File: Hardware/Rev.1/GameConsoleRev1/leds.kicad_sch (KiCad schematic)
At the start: 18 parts

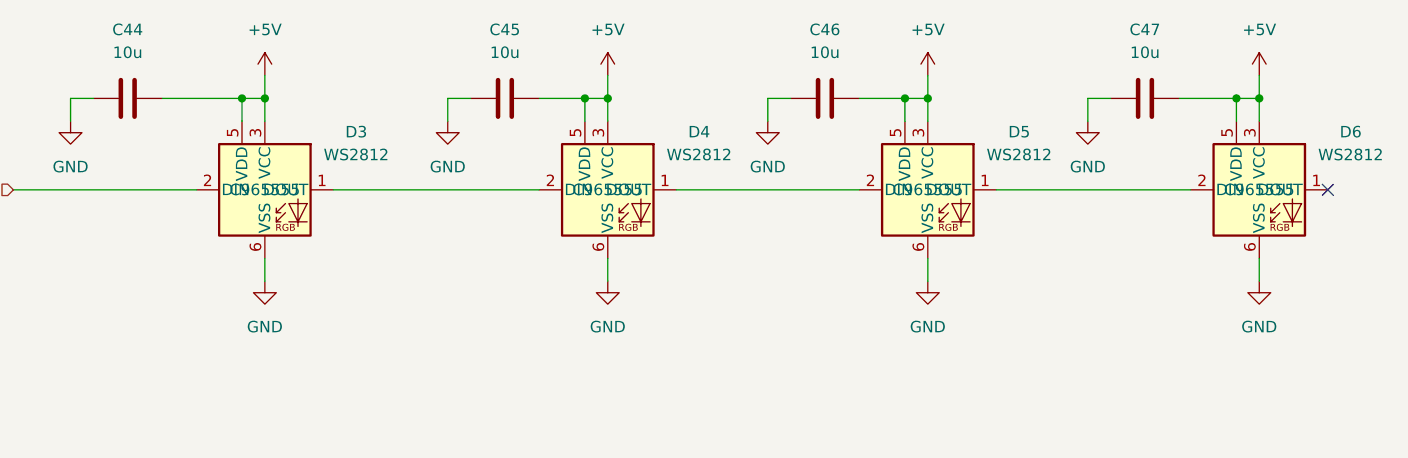
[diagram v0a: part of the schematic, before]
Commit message: Added CPP Build
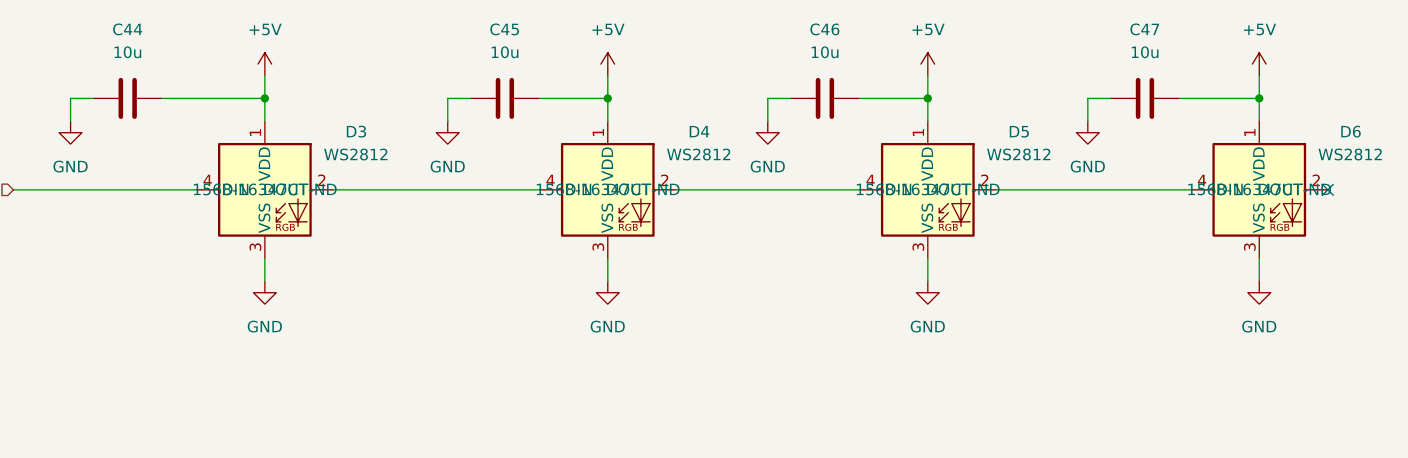
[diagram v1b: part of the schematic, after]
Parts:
- D12: footprint LED_SMD:LED_0603_1608Metric -> LED_SMD:LED_0805_2012Metric; DK# C566D-BFE-CU0W0351-ND -> 3147-B1701USD-20D000114U1930CT-ND
- D13, D14: footprint LED_SMD:LED_0603_1608Metric -> LED_SMD:LED_0805_2012Metric; DK# C566D-BFE-CU0W0351-ND -> 3147-B1701NG--20D000314U1930CT-ND
- D15, D16: footprint LED_SMD:LED_0603_1608Metric -> LED_SMD:LED_0805_2012Metric; DK# C566D-BFE-CU0W0351-ND -> 3147-B1701UD--20D000414U1930CT-ND
- D3, D4, D5, D6: footprint LED_SMD:LED_WS2812_PLCC6_5.0x5.0mm_P1.6mm -> LED_SMD:LED_WS2812B_PLCC4_5.0x5.0mm_P3.2mm; symbol LED:WS2812 -> LED:WS2812B; DK# (none) -> 1568-16347CT-ND; LCSC C965555 -> (none)
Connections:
- net +5V: now also D3.1 (VDD), D4.1 (VDD), D5.1 (VDD), D6.1 (VDD); no longer D3.3 (VCC), D3.5 (VDD), D4.3 (VCC), D4.5 (VDD), D5.3 (VCC), D5.5 (VDD), D6.3 (VCC), D6.5 (VDD)
- net GND: now also D3.3 (VSS), D4.3 (VSS), D5.3 (VSS), D6.3 (VSS); no longer D3.6 (VSS), D4.6 (VSS), D5.6 (VSS), D6.6 (VSS)
- net GPIO6: now also D3.4 (DIN); no longer D3.2 (DIN)
- net at D6.2 (DOUT): no longer D5.1 (DOUT)
- net at D5.2 (DOUT): now also D6.4 (DIN); no longer D4.1 (DOUT)
- net at D5.4 (DIN): now also D4.2 (DOUT)
- net at D4.4 (DIN): now also D3.2 (DOUT)
